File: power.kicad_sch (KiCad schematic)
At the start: 30 parts, among them U5 TI LMR54410DBV, U6 INA3221AIRGV

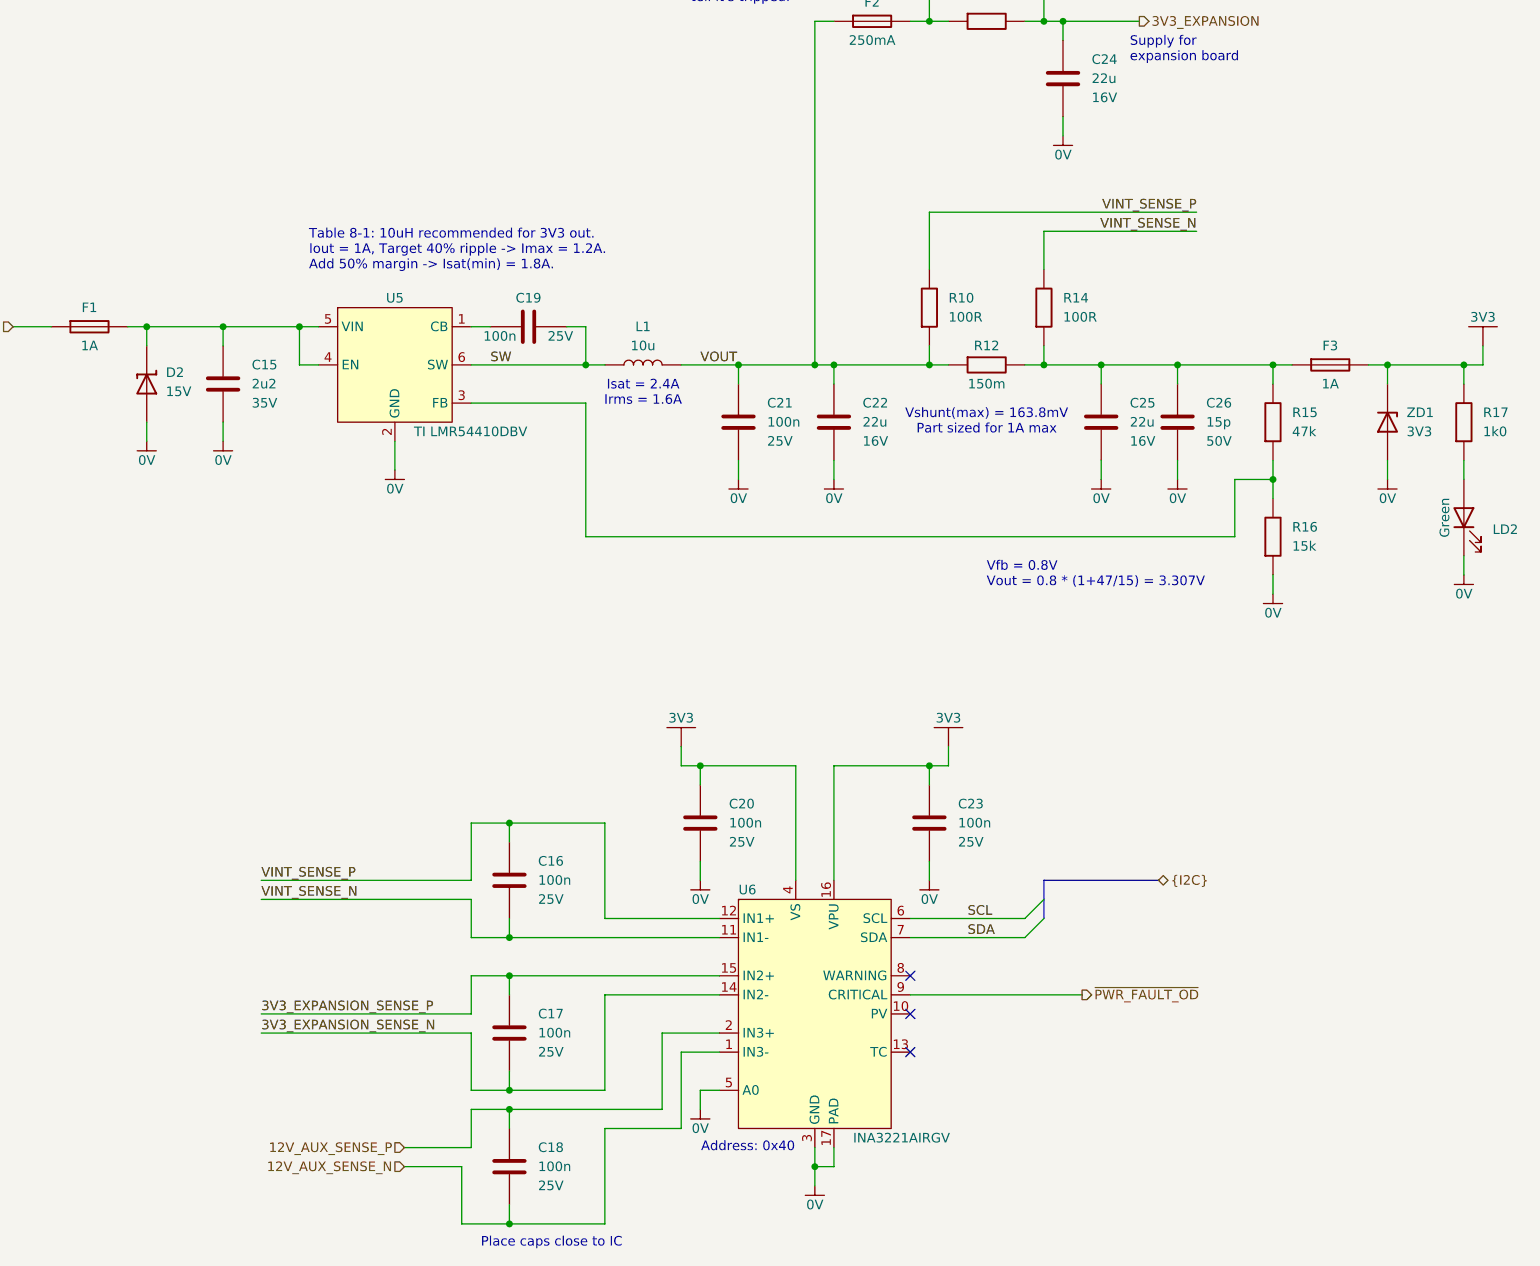
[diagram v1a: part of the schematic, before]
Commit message: started on mcu pinout
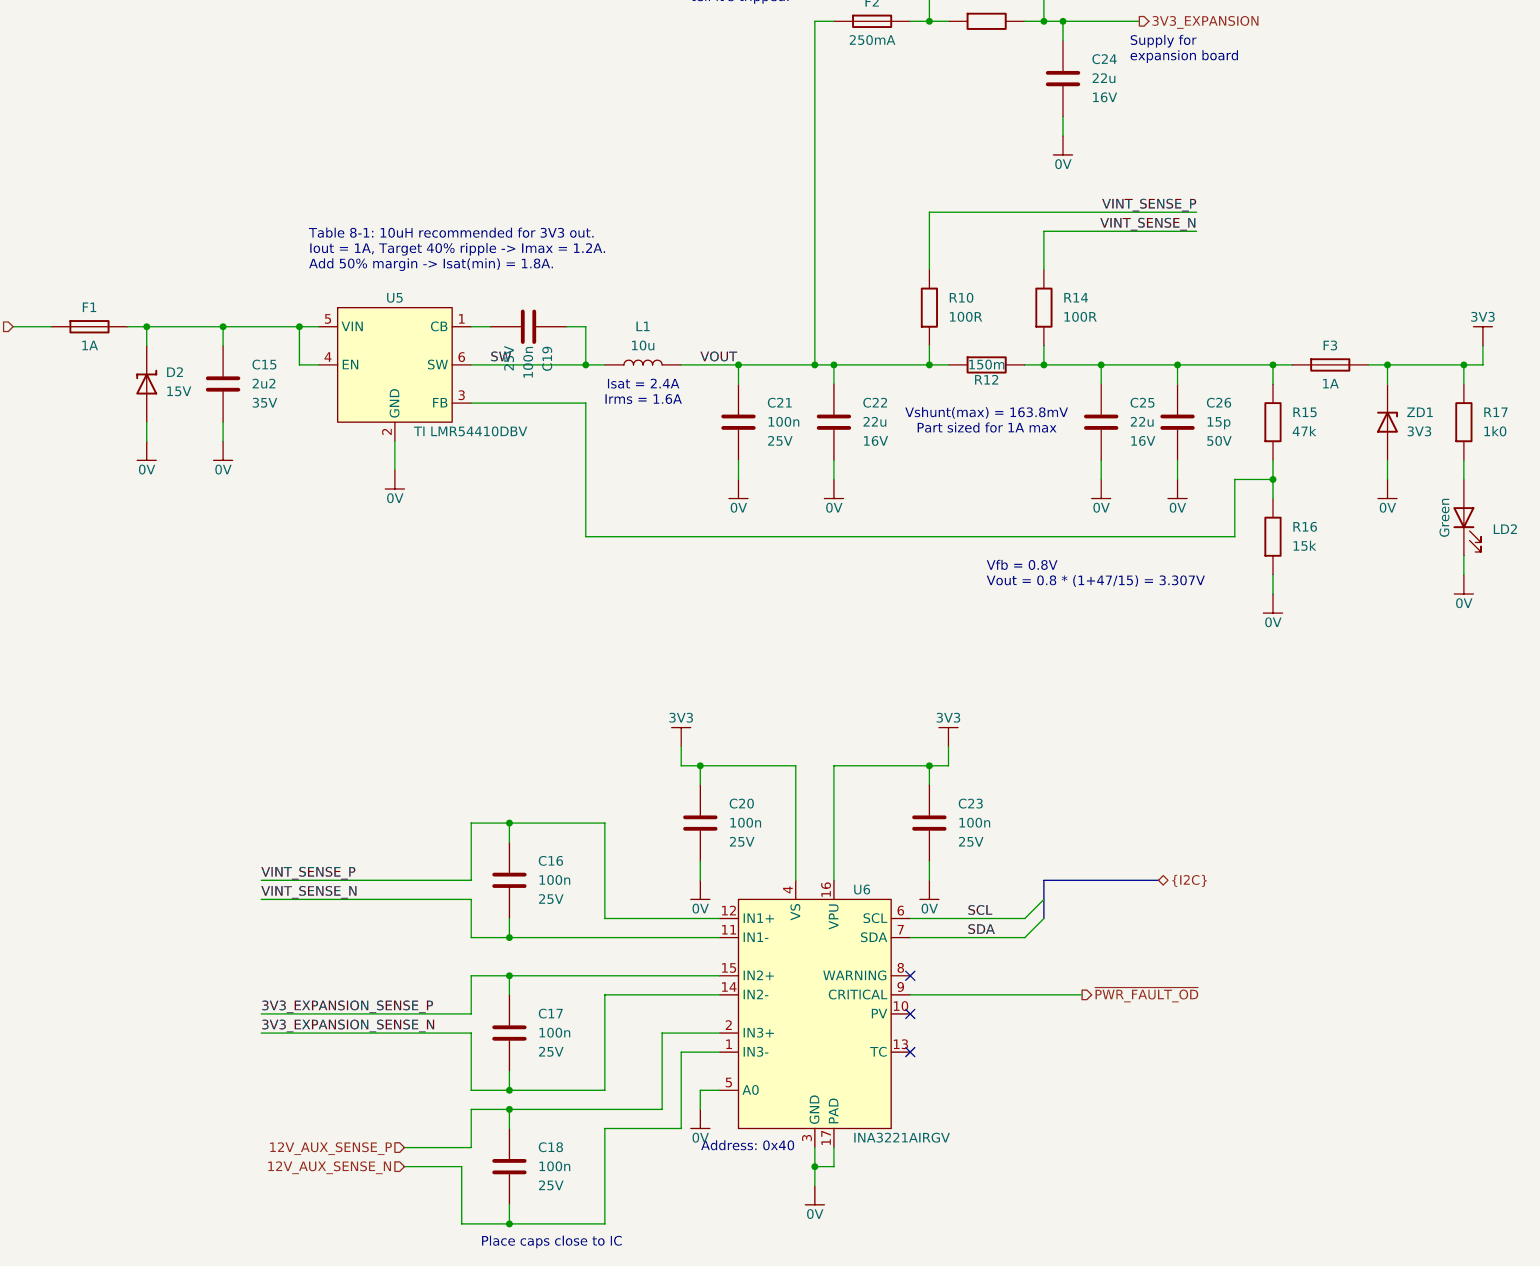
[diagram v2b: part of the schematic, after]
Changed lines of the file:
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@@
 		(dnp no)
 		(property "Reference" "U6"
-			(at 213.36 179.07 0)
+			(at 228.6 179.07 0)
 			(show_name no)
 			(do_not_autoplace yes)
@@
 		(dnp no)
 		(property "Reference" "R12"
-			(at 246.38 106.68 90)
+			(at 246.38 111.252 90)
 			(show_name no)
 			(do_not_autoplace no)
@@
 		)
 		(property "Value" "150m"
-			(at 246.38 111.76 90)
+			(at 246.38 109.22 90)
 			(show_name no)
 			(do_not_autoplace no)
@@
 		(dnp no)
 		(fields_autoplaced yes)
-		(property "Reference" "#PWR038"
+		(property "Reference" "#PWR38"
 			(at 256.54 78.74 0)
 			(hide yes)
@@
 		)
 		(property "Value" "0V"
-			(at 256.54 81.28 0)
+			(at 256.54 82.55 0)
 			(show_name no)
 			(do_not_autoplace yes)
@@
 			(project "P0004-PCB-001"
 				(path "/acdb93e6-9aa6-4a78-8a68-9d0ae3318f45/35d58bcc-6ce4-4583-93f1-63aee4dbfc17"
-					(reference "#PWR038")
+					(reference "#PWR38")
 					(unit 1)
 				)
@@
 		(dnp no)
 		(fields_autoplaced yes)
-		(property "Reference" "#PWR037"
+		(property "Reference" "#PWR37"
 			(at 241.935 163.195 0)
 			(hide yes)
@@
 			(project "P0004-PCB-001"
 				(path "/acdb93e6-9aa6-4a78-8a68-9d0ae3318f45/35d58bcc-6ce4-4583-93f1-63aee4dbfc17"
-					(reference "#PWR037")
+					(reference "#PWR37")
 					(unit 1)
 				)
@@
 		(dnp no)
 		(fields_autoplaced yes)
-		(property "Reference" "#PWR030"
+		(property "Reference" "#PWR30"
 			(at 205.105 163.195 0)
 			(hide yes)
@@
 			(project "P0004-PCB-001"
 				(path "/acdb93e6-9aa6-4a78-8a68-9d0ae3318f45/35d58bcc-6ce4-4583-93f1-63aee4dbfc17"
-					(reference "#PWR030")
+					(reference "#PWR30")
 					(unit 1)
 				)
@@
 		(dnp no)
 		(fields_autoplaced yes)
-		(property "Reference" "#PWR035"
+		(property "Reference" "#PWR35"
 			(at 226.06 124.46 0)
 			(hide yes)
@@
 		)
 		(property "Value" "0V"
-			(at 226.06 127 0)
+			(at 226.06 128.27 0)
 			(show_name no)
 			(do_not_autoplace yes)
@@
 			(project "P0004-PCB-001"
 				(path "/acdb93e6-9aa6-4a78-8a68-9d0ae3318f45/35d58bcc-6ce4-4583-93f1-63aee4dbfc17"
-					(reference "#PWR035")
+					(reference "#PWR35")
 					(unit 1)
 				)
@@
 		(dnp no)
 		(fields_autoplaced yes)
-		(property "Reference" "#PWR032"
+		(property "Reference" "#PWR32"
 			(at 208.28 208.28 0)
 			(hide yes)
@@
 		)
 		(property "Value" "0V"
-			(at 208.28 210.82 0)
+			(at 208.28 212.09 0)
 			(show_name no)
 			(do_not_autoplace yes)
@@
 			(project "P0004-PCB-001"
 				(path "/acdb93e6-9aa6-4a78-8a68-9d0ae3318f45/35d58bcc-6ce4-4583-93f1-63aee4dbfc17"
-					(reference "#PWR032")
+					(reference "#PWR32")
 					(unit 1)
 				)
@@
 		(dnp no)
 		(fields_autoplaced yes)
-		(property "Reference" "#PWR029"
+		(property "Reference" "#PWR29"
 			(at 167.64 123.19 0)
 			(hide yes)
@@
 		)
 		(property "Value" "0V"
-			(at 167.64 125.73 0)
+			(at 167.64 127 0)
 			(show_name no)
 			(do_not_autoplace yes)
@@
 			(project "P0004-PCB-001"
 				(path "/acdb93e6-9aa6-4a78-8a68-9d0ae3318f45/35d58bcc-6ce4-4583-93f1-63aee4dbfc17"
-					(reference "#PWR029")
+					(reference "#PWR29")
 					(unit 1)
 				)
@@
 		(dnp no)
 		(property "Reference" "C19"
-			(at 185.42 100.33 90)
+			(at 187.96 106.68 0)
 			(show_name no)
 			(do_not_autoplace no)
@@
 					(size 1.27 1.27)
 				)
+				(justify left)
 			)
 		)
 		(property "Value" "100n"
-			(at 181.61 105.41 90)
+			(at 185.42 106.68 0)
 			(show_name no)
 			(do_not_autoplace no)
@@
 					(size 1.27 1.27)
 				)
+				(justify left)
 			)
 		)
@@
 		)
 		(property "Voltage" "25V"
-			(at 187.96 105.41 90)
+			(at 182.88 106.68 0)
 			(show_name no)
 			(do_not_autoplace no)
@@
 		(dnp no)
 		(fields_autoplaced yes)
-		(property "Reference" "#PWR027"
+		(property "Reference" "#PWR27"
 			(at 134.62 119.38 0)
 			(hide yes)
@@
 		)
 		(property "Value" "0V"
-			(at 134.62 121.92 0)
+			(at 134.62 123.19 0)
 			(show_name no)
 			(do_not_autoplace yes)
@@
 			(project "P0004-PCB-001"
 				(path "/acdb93e6-9aa6-4a78-8a68-9d0ae3318f45/35d58bcc-6ce4-4583-93f1-63aee4dbfc17"
-					(reference "#PWR027")
+					(reference "#PWR27")
 					(unit 1)
 				)
@@
 		(dnp no)
 		(fields_autoplaced yes)
-		(property "Reference" "#PWR044"
+		(property "Reference" "#PWR44"
 			(at 311.785 109.855 0)
 			(hide yes)
@@
 			(project "P0004-PCB-001"
 				(path "/acdb93e6-9aa6-4a78-8a68-9d0ae3318f45/35d58bcc-6ce4-4583-93f1-63aee4dbfc17"
-					(reference "#PWR044")
+					(reference "#PWR44")
 					(unit 1)
 				)
@@
 		(dnp no)
 		(fields_autoplaced yes)
-		(property "Reference" "#PWR041"
+		(property "Reference" "#PWR41"
 			(at 284.48 139.7 0)
 			(hide yes)
@@
 		)
 		(property "Value" "0V"
-			(at 284.48 142.24 0)
+			(at 284.48 143.51 0)
 			(show_name no)
 			(do_not_autoplace yes)
@@
 			(project "P0004-PCB-001"
 				(path "/acdb93e6-9aa6-4a78-8a68-9d0ae3318f45/35d58bcc-6ce4-4583-93f1-63aee4dbfc17"
-					(reference "#PWR041")
+					(reference "#PWR41")
 					(unit 1)
 				)
@@
 		(dnp no)
 		(fields_autoplaced yes)
-		(property "Reference" "#PWR036"
+		(property "Reference" "#PWR36"
 			(at 238.76 177.8 0)
 			(hide yes)
@@
 		)
 		(property "Value" "0V"
-			(at 238.76 180.34 0)
+			(at 238.76 181.61 0)
 			(show_name no)
 			(do_not_autoplace yes)
@@
 			(project "P0004-PCB-001"
 				(path "/acdb93e6-9aa6-4a78-8a68-9d0ae3318f45/35d58bcc-6ce4-4583-93f1-63aee4dbfc17"
-					(reference "#PWR036")
+					(reference "#PWR36")
 					(unit 1)
 				)
@@
 		(dnp no)
 		(fields_autoplaced yes)
-		(property "Reference" "#PWR040"
+		(property "Reference" "#PWR40"
 			(at 271.78 124.46 0)
 			(hide yes)
@@
 		)
 		(property "Value" "0V"
-			(at 271.78 127 0)
+			(at 271.78 128.27 0)
 			(show_name no)
 			(do_not_autoplace yes)
@@
 			(project "P0004-PCB-001"
 				(path "/acdb93e6-9aa6-4a78-8a68-9d0ae3318f45/35d58bcc-6ce4-4583-93f1-63aee4dbfc17"
-					(reference "#PWR040")
+					(reference "#PWR40")
 					(unit 1)
 				)
@@
 		(dnp no)
 		(fields_autoplaced yes)
-		(property "Reference" "#PWR028"
+		(property "Reference" "#PWR28"
 			(at 144.78 119.38 0)
 			(hide yes)
@@
 		)
 		(property "Value" "0V"
-			(at 144.78 121.92 0)
+			(at 144.78 123.19 0)
 			(show_name no)
 			(do_not_autoplace yes)
@@
 			(project "P0004-PCB-001"
 				(path "/acdb93e6-9aa6-4a78-8a68-9d0ae3318f45/35d58bcc-6ce4-4583-93f1-63aee4dbfc17"
-					(reference "#PWR028")
+					(reference "#PWR28")
 					(unit 1)
 				)
@@
 		(dnp no)
 		(fields_autoplaced yes)
-		(property "Reference" "#PWR039"
+		(property "Reference" "#PWR39"
 			(at 261.62 124.46 0)
 			(hide yes)
@@
 		)
 		(property "Value" "0V"
-			(at 261.62 127 0)
+			(at 261.62 128.27 0)
 			(show_name no)
 			(do_not_autoplace yes)
@@
 			(project "P0004-PCB-001"
 				(path "/acdb93e6-9aa6-4a78-8a68-9d0ae3318f45/35d58bcc-6ce4-4583-93f1-63aee4dbfc17"
-					(reference "#PWR039")
+					(reference "#PWR39")
 					(unit 1)
 				)
@@
 		(dnp no)
 		(fields_autoplaced yes)
-		(property "Reference" "#PWR031"
+		(property "Reference" "#PWR31"
 			(at 208.28 177.8 0)
 			(hide yes)
@@
 		)
 		(property "Value" "0V"
-			(at 208.28 180.34 0)
+			(at 208.28 181.61 0)
 			(show_name no)
 			(do_not_autoplace yes)
@@
 			(project "P0004-PCB-001"
 				(path "/acdb93e6-9aa6-4a78-8a68-9d0ae3318f45/35d58bcc-6ce4-4583-93f1-63aee4dbfc17"
-					(reference "#PWR031")
+					(reference "#PWR31")
 					(unit 1)
 				)
@@
 		(dnp no)
 		(fields_autoplaced yes)
-		(property "Reference" "#PWR043"
+		(property "Reference" "#PWR43"
 			(at 309.88 137.16 0)
 			(hide yes)
@@
 		)
 		(property "Value" "0V"
-			(at 309.88 139.7 0)
+			(at 309.88 140.97 0)
 			(show_name no)
 			(do_not_autoplace yes)
@@
 			(project "P0004-PCB-001"
 				(path "/acdb93e6-9aa6-4a78-8a68-9d0ae3318f45/35d58bcc-6ce4-4583-93f1-63aee4dbfc17"
-					(reference "#PWR043")
+					(reference "#PWR43")
 					(unit 1)
 				)
@@
 		(dnp no)
 		(fields_autoplaced yes)
-		(property "Reference" "#PWR034"
+		(property "Reference" "#PWR34"
 			(at 223.52 218.44 0)
 			(hide yes)
@@
 		)
 		(property "Value" "0V"
-			(at 223.52 220.98 0)
+			(at 223.52 222.25 0)
 			(show_name no)
 			(do_not_autoplace yes)
@@
 			(project "P0004-PCB-001"
 				(path "/acdb93e6-9aa6-4a78-8a68-9d0ae3318f45/35d58bcc-6ce4-4583-93f1-63aee4dbfc17"
-					(reference "#PWR034")
+					(reference "#PWR34")
 					(unit 1)
 				)
@@
 		(dnp no)
 		(fields_autoplaced yes)
-		(property "Reference" "#PWR042"
+		(property "Reference" "#PWR42"
 			(at 299.72 124.46 0)
 			(hide yes)
@@
 		)
 		(property "Value" "0V"
-			(at 299.72 127 0)
+			(at 299.72 128.27 0)
 			(show_name no)
 			(do_not_autoplace yes)
@@
 			(project "P0004-PCB-001"
 				(path "/acdb93e6-9aa6-4a78-8a68-9d0ae3318f45/35d58bcc-6ce4-4583-93f1-63aee4dbfc17"
-					(reference "#PWR042")
+					(reference "#PWR42")
 					(unit 1)
 				)
@@
 		(dnp no)
 		(fields_autoplaced yes)
-		(property "Reference" "#PWR033"
+		(property "Reference" "#PWR33"
 			(at 213.36 124.46 0)
 			(hide yes)
@@
 		)
 		(property "Value" "0V"
-			(at 213.36 127 0)
+			(at 213.36 128.27 0)
 			(show_name no)
 			(do_not_autoplace yes)
@@
 			(project "P0004-PCB-001"
 				(path "/acdb93e6-9aa6-4a78-8a68-9d0ae3318f45/35d58bcc-6ce4-4583-93f1-63aee4dbfc17"
-					(reference "#PWR033")
+					(reference "#PWR33")
 					(unit 1)
 				)

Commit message: layout progress
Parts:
- added LD3: Red, LED_SMD:LED_0603_1608Metric, symbol aaa_led_auto_wut:Lite-On_LTST-C193KRKT-5A
- added R24: 1k0, Resistor_WUT:R_0402_1005Metric, symbol aaa_resistor_auto_wut:KOA Speer RK73H1ETTP1001F
- added R25: 10k, Resistor_WUT:R_0402_1005Metric, symbol aaa_resistor_auto_wut:KOA Speer RK73H1ETTP1002F
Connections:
- net 12V_AUX_SENSE_N: now also C16.2, U6.11 (IN1-); no longer C18.2, U6.1 (IN3-)
- net 12V_AUX_SENSE_P: now also C16.1, U6.12 (IN1+); no longer C18.1, U6.2 (IN3+)
- net 3V3: now also R24.1, R25.1
- net 3V3_EXPANSION_SENSE_N: now also C18.2, U6.1 (IN3-); no longer C17.2, U6.14 (IN2-)
- net 3V3_EXPANSION_SENSE_P: now also C18.1, U6.2 (IN3+); no longer C17.1, U6.15 (IN2+)
- net VINT_SENSE_N: now also C17.2, U6.14 (IN2-); no longer C16.2, U6.11 (IN1-)
- net VINT_SENSE_P: now also C17.1, U6.15 (IN2+); no longer C16.1, U6.12 (IN1+)
- net ~{PWR_FAULT_OD}: now also LD3.1 (K), R25.2
- new net: LD3.2 (A), R24.2
